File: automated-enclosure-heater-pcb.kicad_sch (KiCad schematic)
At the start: 61 parts, among them J1 PowerPole Power in, J2 Servo, J3 RJ45, J4 Buttons, J5 DS18B20 Heater, J6 DS18B20 Case, J7 PowerPole Heater Connector, J8 JST-XH Fan Connector, K1 G5LE-1A, K2 G5LE-1A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

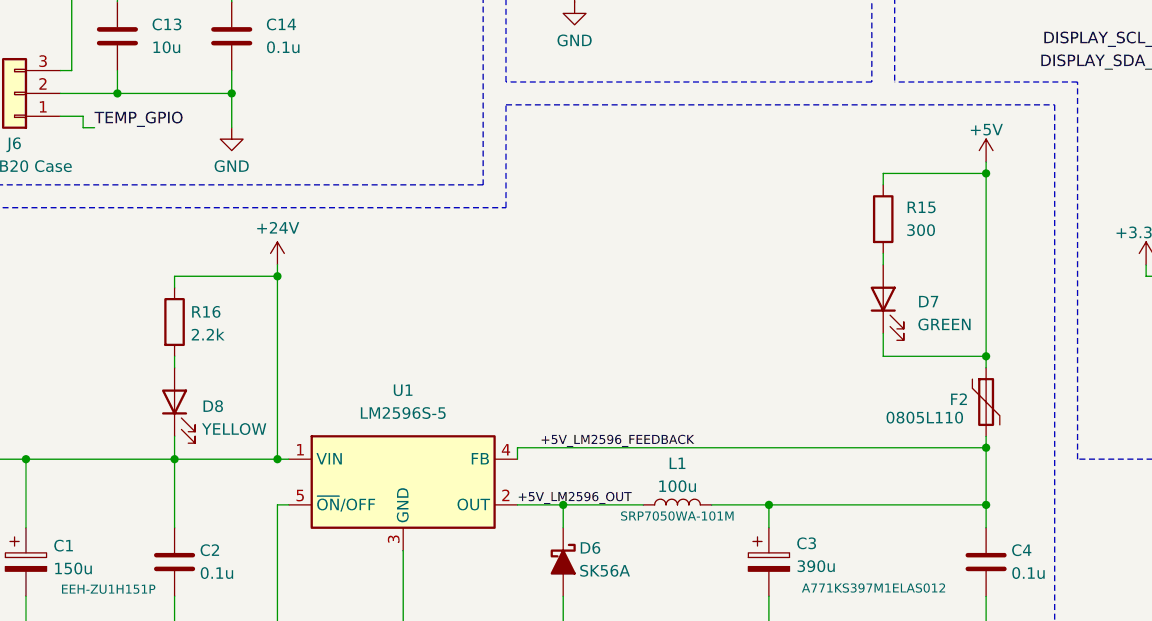
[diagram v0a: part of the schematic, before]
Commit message: Fix LED issue
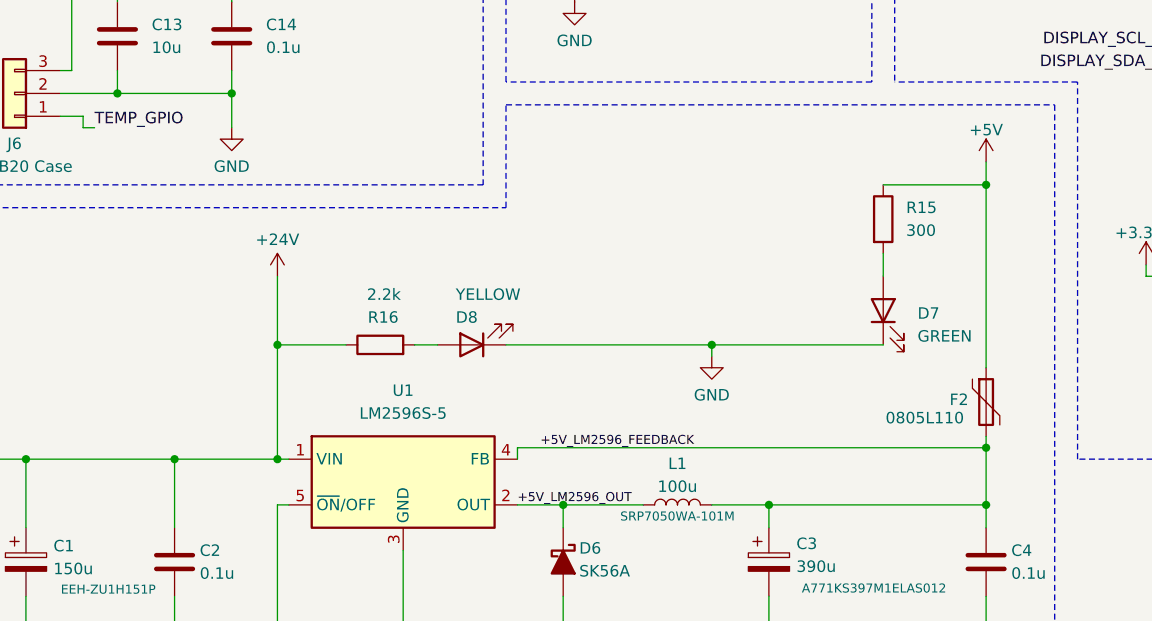
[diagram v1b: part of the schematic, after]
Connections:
- net +24V: no longer D8.1 (K)
- net +5V: no longer D7.1 (K)
- net GND: now also D7.1 (K), D8.1 (K)
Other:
- moved on the sheet: D7, D8, R16

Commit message: Add minor silkscreen adjustments
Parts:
- D2: Purpose (none) -> HEATER
- D3: Purpose (none) -> FAN
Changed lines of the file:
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@@
+			)
+		)
+		(property "Purpose" "HEATER"
+			(at 181.356 57.15 90)
+			(effects
+				(font
+					(size 1.27 1.27)
+				)
 			)
 		)
@@
 			)
 		)
+		(property "Purpose" "FAN"
+			(at 236.728 57.15 90)
+			(effects
+				(font
+					(size 1.27 1.27)
+				)
+			)
+		)

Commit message: Fix DISP pinout
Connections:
- net DISPLAY_SDA_OUT: now also J3.2; no longer J3.1
- net GND: now also J3.1; no longer J3.2
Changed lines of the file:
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@@
-	)
-	(junction
-		(at 35.56 45.72)
-		(diameter 0)
-		(color 0 0 0 0)
 	)
 	(junction
@@
 	)
 	(junction
+		(at 35.56 48.26)
+		(diameter 0)
+		(color 0 0 0 0)
+	)
+	(junction
 		(at 80.01 93.98)
 		(diameter 0)
@@
 	(wire
 		(pts
-			(xy 35.56 43.18) (xy 35.56 45.72)
+			(xy 35.56 43.18) (xy 35.56 48.26)
 		)
 		(stroke
@@
 	(wire
 		(pts
+			(xy 34.29 48.26) (xy 35.56 48.26)
+		)
+		(stroke
+			(width 0)
+			(type default)
+		)
+	)
+	(wire
+		(pts
 			(xy 43.18 24.13) (xy 39.37 24.13)
 		)
@@
 	(wire
 		(pts
+			(xy 34.29 45.72) (xy 57.15 45.72)
+		)
+		(stroke
+			(width 0)
+			(type default)
+		)
+	)
+	(wire
+		(pts
 			(xy 200.66 58.42) (xy 200.66 62.23)
 		)
@@
 	(wire
 		(pts
-			(xy 34.29 45.72) (xy 35.56 45.72)
-		)
-		(stroke
-			(width 0)
-			(type default)
-		)
-	)
-	(wire
-		(pts
 			(xy 242.57 52.07) (xy 242.57 58.42)
 		)
@@
 	(wire
 		(pts
-			(xy 57.15 58.42) (xy 57.15 48.26)
+			(xy 57.15 58.42) (xy 57.15 45.72)
 		)
 		(stroke
@@
 	(wire
 		(pts
-			(xy 35.56 45.72) (xy 35.56 50.8)
-		)
-		(stroke
-			(width 0)
-			(type default)
-		)
-	)
-	(wire
-		(pts
 			(xy 43.18 24.13) (xy 43.18 25.4)
 		)
@@
 	(wire
 		(pts
+			(xy 35.56 48.26) (xy 35.56 50.8)
+		)
+		(stroke
+			(width 0)
+			(type default)
+		)
+	)
+	(wire
+		(pts
 			(xy 121.92 185.42) (xy 144.78 185.42)
 		)
@@
 		(pts
 			(xy 29.21 128.27) (xy 29.21 127)
-		)
-		(stroke
-			(width 0)
-			(type default)
-		)
-	)
-	(wire
-		(pts
-			(xy 34.29 48.26) (xy 57.15 48.26)
 		)
 		(stroke
@@
 	)
 	(label "DISPLAY_SDA_OUT"
-		(at 39.37 48.26 0)
+		(at 39.37 45.72 0)
 		(fields_autoplaced yes)
 		(effects

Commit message: Adjust Arduino pinout and push version to v0.2
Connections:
- net BUTTON_DOWN_GPIO: now also A1.D2; no longer A1.D4
- net BUTTON_UP_GPIO: now also A1.D4; no longer A1.D2
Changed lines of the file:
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@@
 	(title_block
 		(title "Automated Enclosure Heater PCB")
-		(date "2024-03-24")
-		(rev "v0.1")
+		(date "2024-04-07")
+		(rev "v0.2")
 		(comment 1 "Author: Timo Tomasini")
 	)
@@
 	(wire
 		(pts
+			(xy 245.11 106.68) (xy 247.65 106.68)
+		)
+		(stroke
+			(width 0)
+			(type default)
+		)
+	)
+	(wire
+		(pts
 			(xy 208.28 26.67) (xy 208.28 27.94)
 		)
@@
 	(wire
 		(pts
-			(xy 247.65 109.22) (xy 245.11 109.22)
-		)
-		(stroke
-			(width 0)
-			(type default)
-		)
-	)
-	(wire
-		(pts
 			(xy 210.82 25.4) (xy 210.82 26.67)
 		)
@@
 	(wire
 		(pts
-			(xy 247.65 104.14) (xy 245.11 104.14)
-		)
-		(stroke
-			(width 0)
-			(type default)
-		)
-	)
-	(wire
-		(pts
 			(xy 104.14 175.26) (xy 104.14 185.42)
 		)
@@
 		)
 	)
-	(wire
-		(pts
-			(xy 247.65 106.68) (xy 245.11 106.68)
-		)
-		(stroke
-			(width 0)
-			(type default)
-		)
-	)
 	(polyline
 		(pts
@@
 	(wire
 		(pts
+			(xy 245.11 109.22) (xy 247.65 109.22)
+		)
+		(stroke
+			(width 0)
+			(type default)
+		)
+	)
+	(wire
+		(pts
 			(xy 148.59 36.83) (xy 148.59 40.64)
 		)
@@
 		(pts
 			(xy 138.43 152.4) (xy 157.48 152.4)
+		)
+		(stroke
+			(width 0)
+			(type default)
+		)
+	)
+	(wire
+		(pts
+			(xy 245.11 104.14) (xy 247.65 104.14)
 		)
 		(stroke
@@
 	)
 	(label "BUTTON_UP_GPIO"
-		(at 247.65 104.14 0)
+		(at 247.65 109.22 0)
 		(fields_autoplaced yes)
 		(effects
@@
 	)
 	(label "BUTTON_DOWN_GPIO"
-		(at 247.65 109.22 0)
+		(at 247.65 104.14 0)
 		(fields_autoplaced yes)
 		(effects

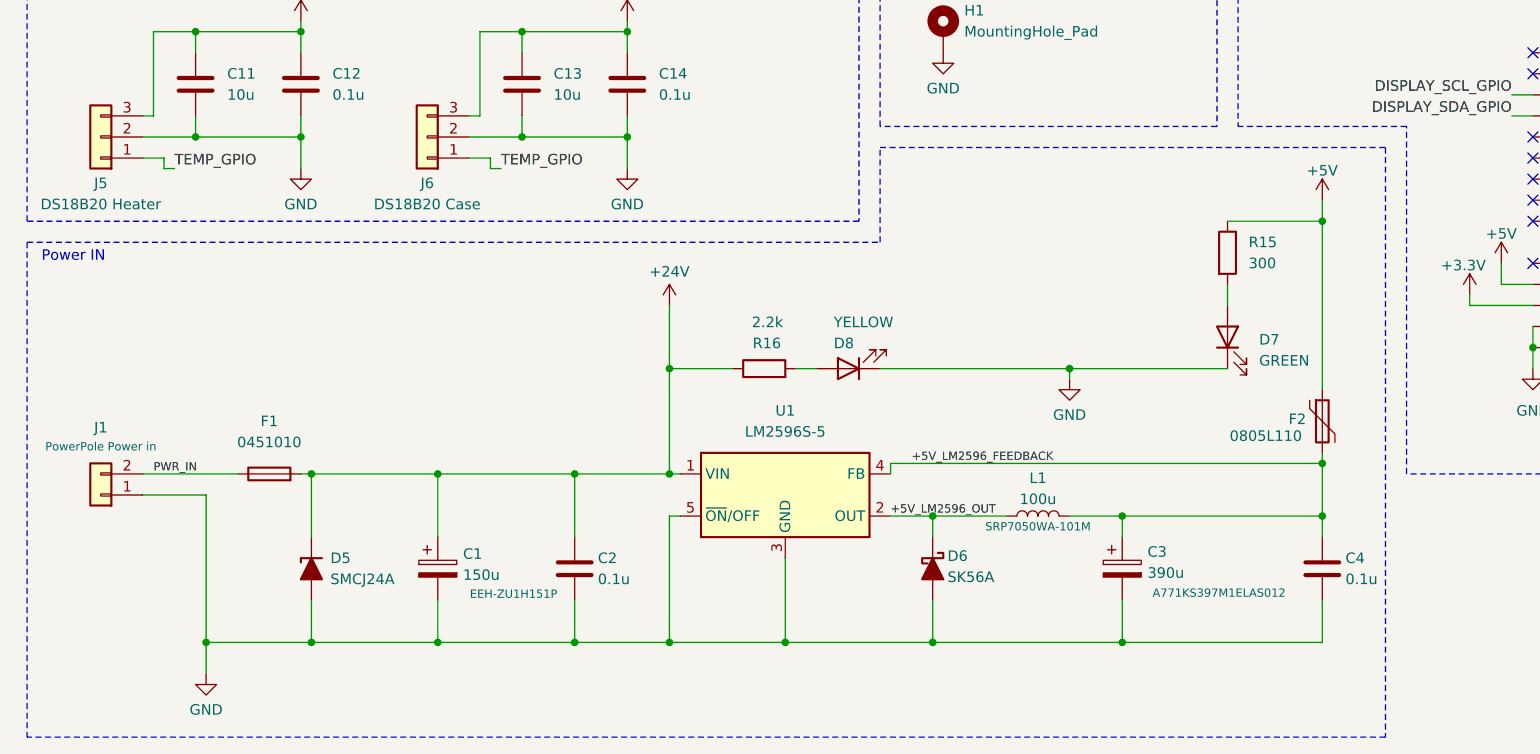
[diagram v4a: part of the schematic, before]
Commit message: Add second resistor for 24V LED and adjust power plane size
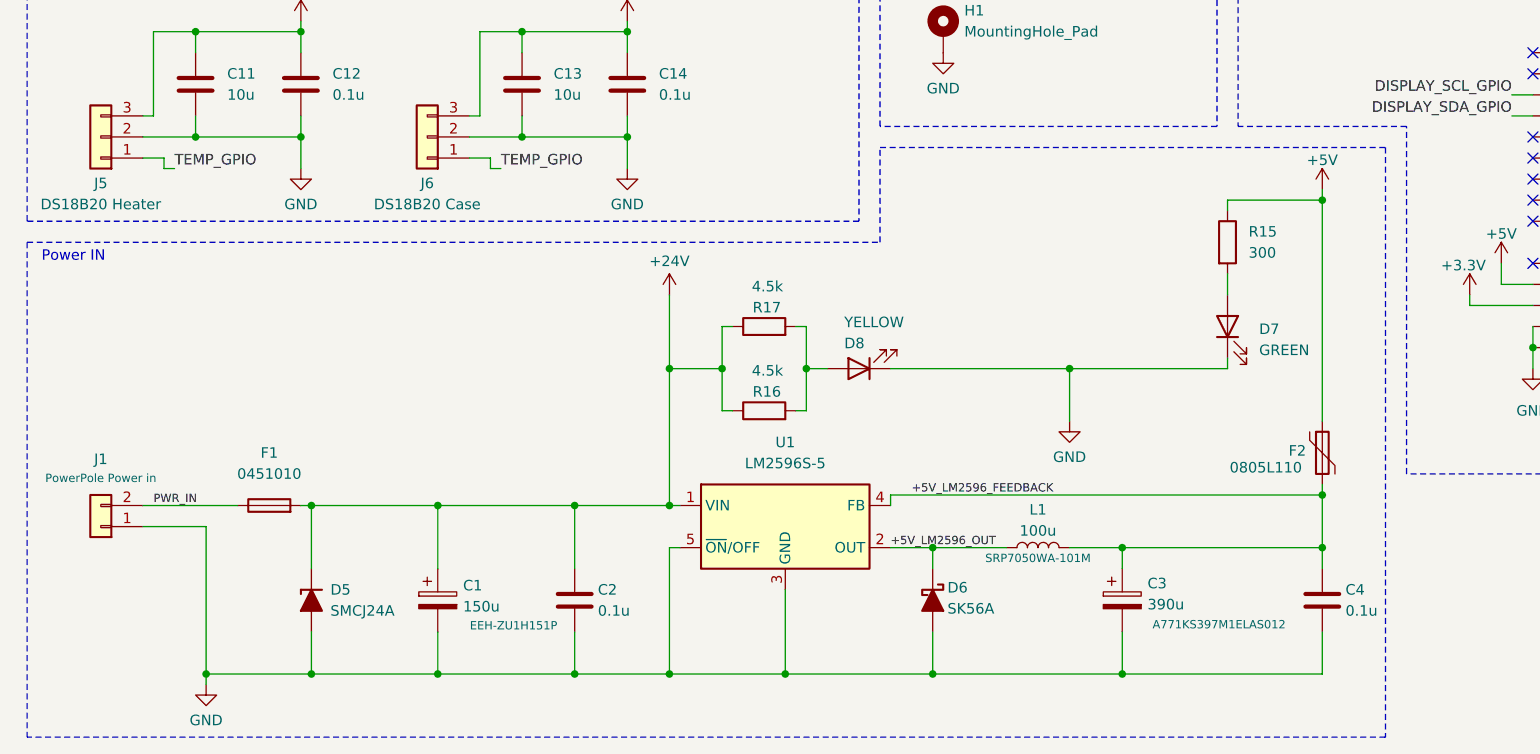
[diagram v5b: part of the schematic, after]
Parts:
- added R17: 4.5k, Resistor_SMD:R_0805_2012Metric, symbol Device:R
- R16: value 2.2k -> 4.5k
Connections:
- net +24V: now also R17.1
- net at D8.2 (A), R16.2: now also R17.2
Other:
- moved on the sheet: C1, C2, C3, C4, D5, D6, D7, D8, F1, F2, J1, L1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
